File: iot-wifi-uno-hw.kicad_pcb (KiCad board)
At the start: 2 copper layers, 68.6 x 53.3 mm, 65 parts, among them CON1 BARREL_JACK, P1 CONN_01X08, P2 CONN_01X08, P3 CONN_01X06, P4 CONN_01X10, P5 CONN_01X04, Q1 Q_NPN_CBE, Q2 Q_NPN_CBE, U1 usb_mini_b, U2 BD00GA5WEFJ, U3 MCP16311-MNY, U4 CH340G, U5 ESP-12E, U6 MCP6001R, U7 MOSFET-P, X1 CRYSTAL_ABM3C

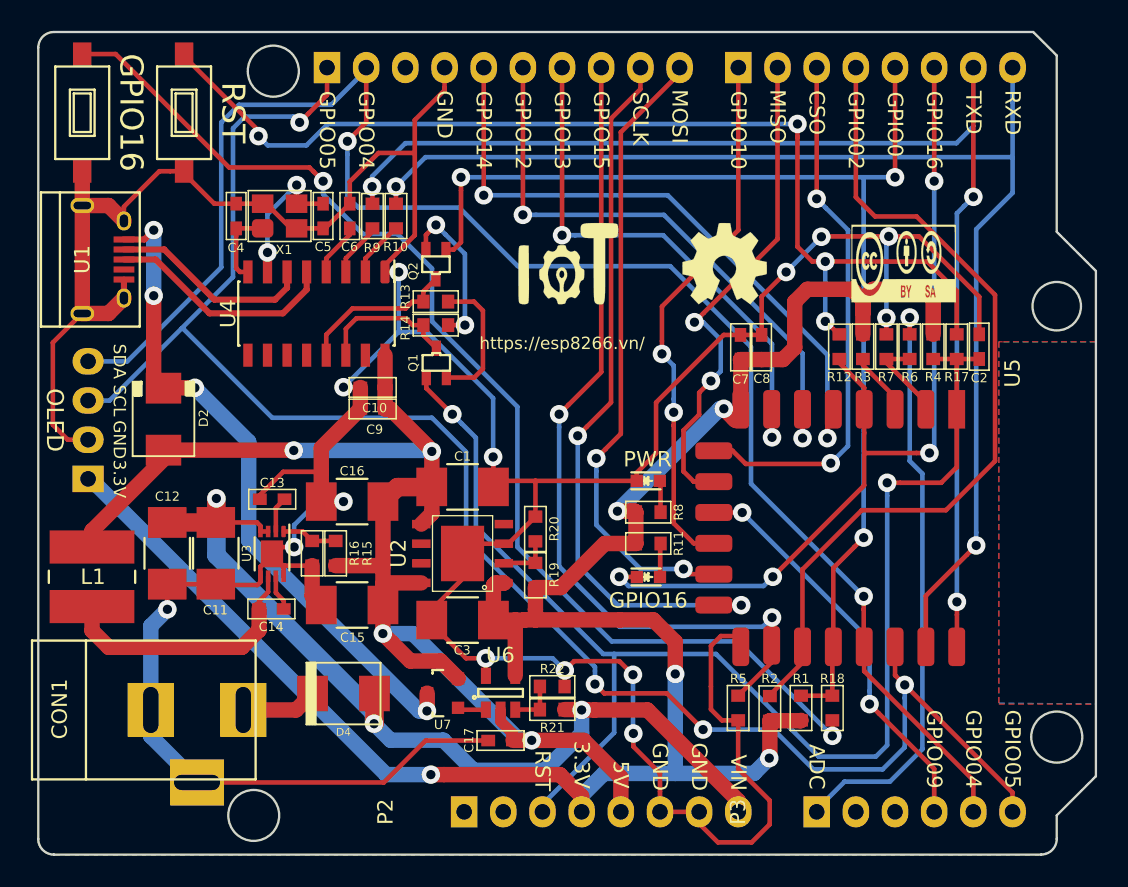
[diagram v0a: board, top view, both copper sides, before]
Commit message: modify lodo IoT & link esp8266.vn and add gerber file
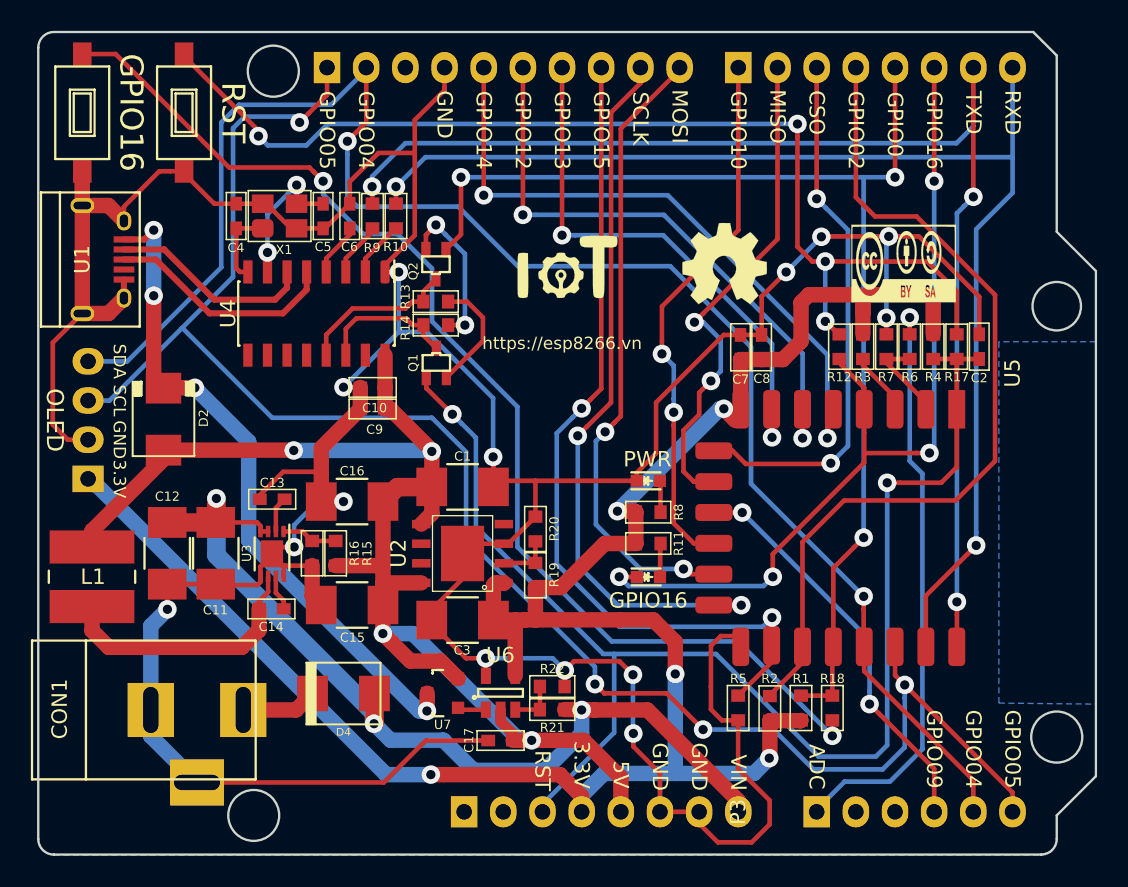
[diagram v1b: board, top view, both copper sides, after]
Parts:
- removed the G*** at (143.8, 73.7)
- added G***: LOGO, ESP8266:logo_iotmake_7.5x5mm, F.Cu at (143.8, 73.9)
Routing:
- net Net-(Q1-Pad2): track 8.88 -> 7.57 mm
- net GPIO2: track 55.3 -> 56.4 mm
- net +3V3: track 138.1 -> 137.3 mm
- removed copper zone on F.Cu, net GND
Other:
- board text added: "https://esp8266.vn"
- board text removed: "https://esp8266.vn/"

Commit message: update gerber file
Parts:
- removed the G*** at (143.8, 73.9)
- removed the G*** at (165.7, 73.7)
- added G***: LOGO, ESP8266:logo-iotmakervn_7, F.Cu at (110.7, 83.8)
- added G***: LOGO, ESP8266:logo-jack-5528, F.Cu at (113.7, 110.6)
- added G***: LOGO, ESP8266:LEDPWR, F.Cu at (149.1, 86.4)
- added G***: LOGO, ESP8266:GPIO16, F.Cu at (149.1, 95.4)
- added G***: LOGO, ESP8266:GPIO0, F.Cu at (115.3, 63.9)
- added G***: LOGO, ESP8266:RST, F.Cu at (122.0, 63.9)
- added G***: LOGO, ESP8266:logo-jack_7.4x3, F.Cu at (113.9, 108.4)
- added G***: LOGO, ESP8266:logo-iotmakervn_7.5x5, F.Cu at (148.2, 70.9)
- added G***: LOGO, ESP8266:logo_cc-bby-sa_14.1x5mm, F.Cu at (168.1, 71.0)
- moved G*** 3.40 mm to (156.1, 71.1)
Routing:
- added copper zone on F.Cu, net GND
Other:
- board text removed: "OLED"
- board text removed: "PWR"
